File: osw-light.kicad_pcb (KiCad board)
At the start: 4 copper layers, 36.1 x 36.1 mm, 55 parts, among them J1 Conn_01x02, Q1 2N7002, SW1 SW_Push, SW2 SW_Push, SW4 SW_Push, SW5 SW_Push, U1 DS3231MZ, U10 XC6209, U11 MCP73831T-2ACI_OT, U13 XC6209, U2 BMA400, U4 GC9A01_IPS_display, U5 USB-OTG, U6 CH340E, U7 ttgo-32-micro, U9 TPS2115A

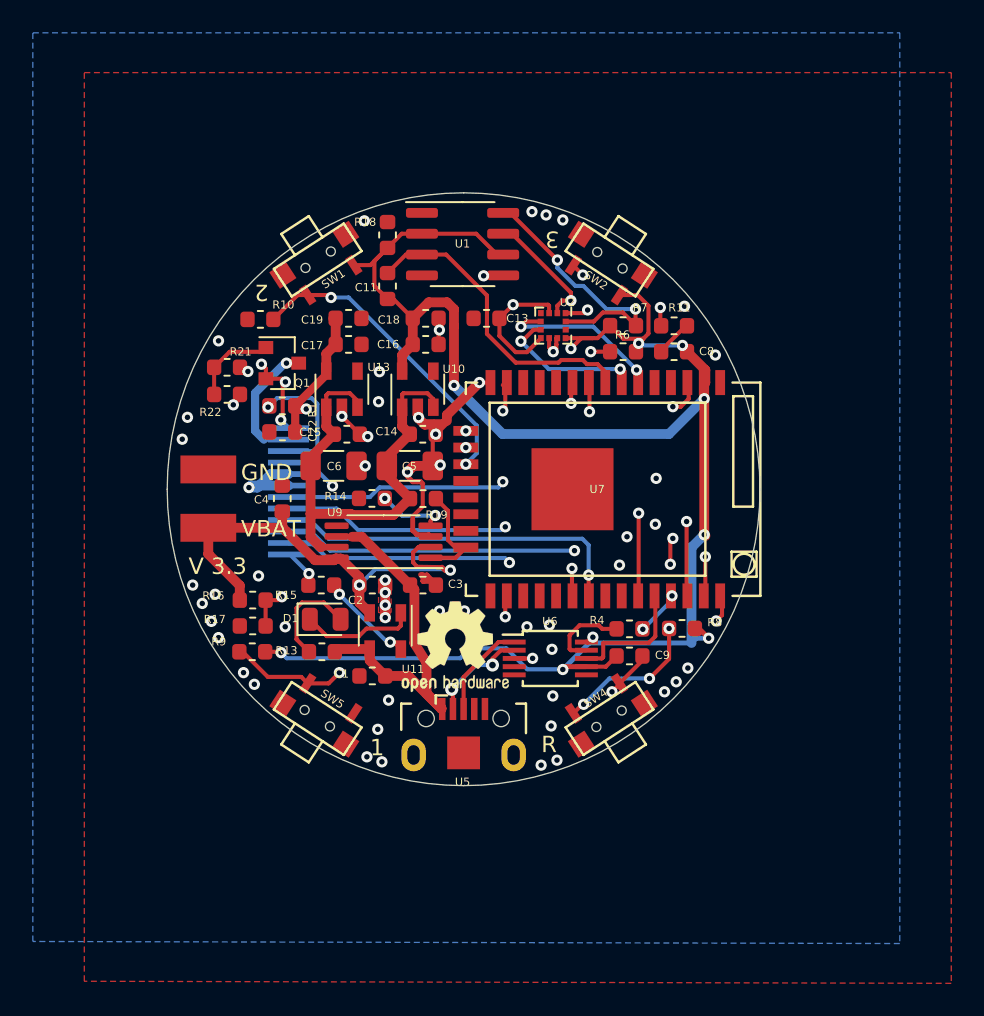
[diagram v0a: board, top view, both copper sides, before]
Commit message: WIP. Move ESP32 to board
PCB Still in progress. Work on hold.
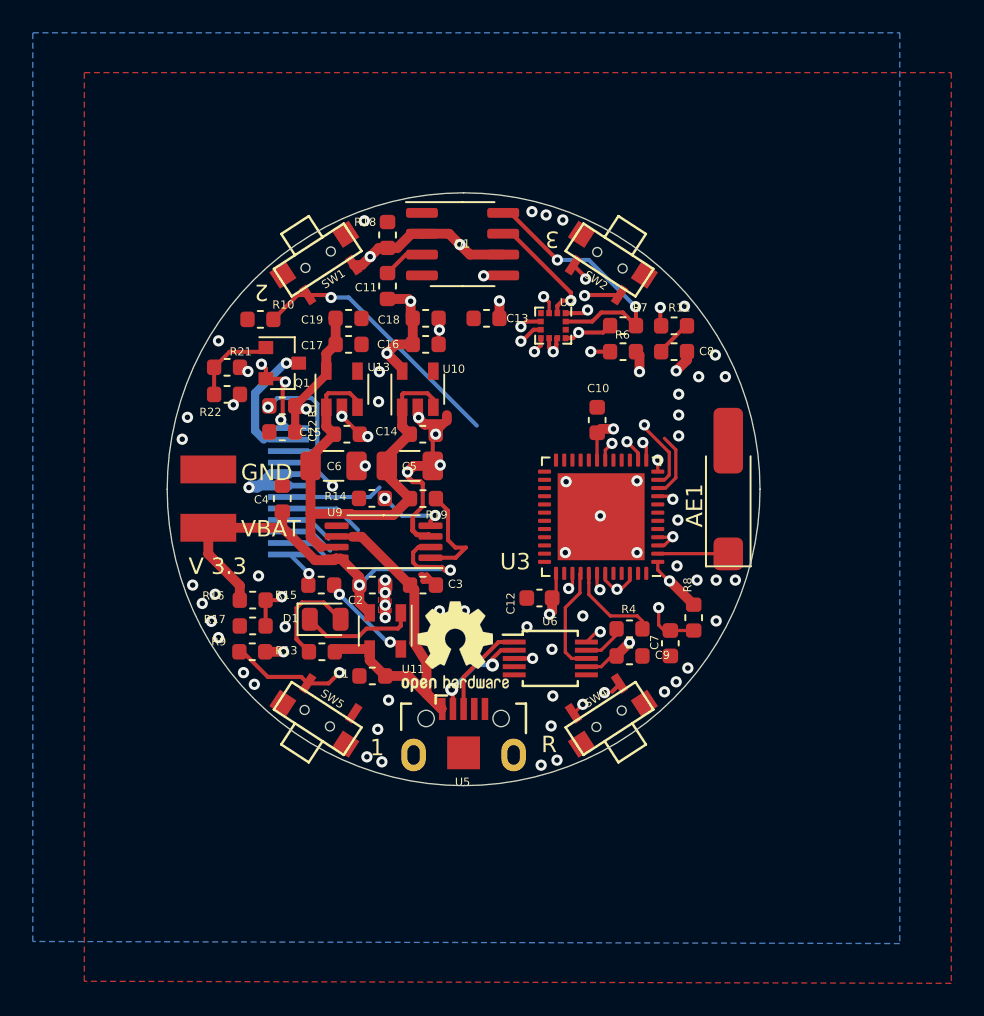
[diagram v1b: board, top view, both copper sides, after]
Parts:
- removed U7: ttgo-32-micro, open-Smartwatch:ttgo-32-micro
- added AE1: Antenna_Chip, open-Smartwatch:Johanson_2450AT42A100, F.Cu at (92.3, 102.6)
- added C10: 4.7u, Capacitor_SMD:C_0603_1608Metric, F.Cu at (84.3, 97.4)
- added C12: 4.7u, Capacitor_SMD:C_0603_1608Metric, F.Cu at (80.8, 108.2)
- added C7: 0.1u, Capacitor_SMD:C_0603_1608Metric, F.Cu at (88.8, 111.0)
- added U3: ESP32-PICO-D4, Package_DFN_QFN:QFN-48-1EP_7x7mm_P0.5mm_EP5.3x5.3mm, F.Cu at (84.6, 103.3)
- moved R8 0.97 mm to (90.2, 109.4), turned to 270 degrees
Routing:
- net +3V3: track 126.3 -> 49.3 mm, vias 11 -> 19
- net /TFT_RST: track 29.6 -> 3.89 mm, vias 2 -> 1
- net /MOSI: track 28.4 -> 3.02 mm, vias 2 -> 0
- net /B_MON: track 26.9 -> 4.05 mm
- net /SCK: track 22.0 -> 2.92 mm, vias 1 -> 0
- net /SDA: track 28.4 -> 9.76 mm
- net /SCL: track 35.5 -> 17.5 mm
- net /TFT_CS: track 20.6 -> 4.79 mm, vias 2 -> 0
- net /RTC_INT: track 18.9 -> 3.28 mm, vias 0 -> 1
- net /BTN3: track 22.8 -> 7.57 mm, vias 3 -> 2
- net /TFT_DC: track 19.8 -> 6.98 mm, vias 2 -> 1
- net /FLASH: track 20.0 -> 7.17 mm, vias 2 -> 1
- net GND: track 64.5 -> 57.5 mm, vias 65 -> 75
- net /EN: track 25.2 -> 20.0 mm, vias 6 -> 3
- net /IO34: track 10.3 -> 5.39 mm, vias 2 -> 1
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- added copper zone on In1.Cu, net +3V3
